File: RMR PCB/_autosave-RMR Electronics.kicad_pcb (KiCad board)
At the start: 2 copper layers, 19 parts, among them J4 RMotor, J8 RMotor Control

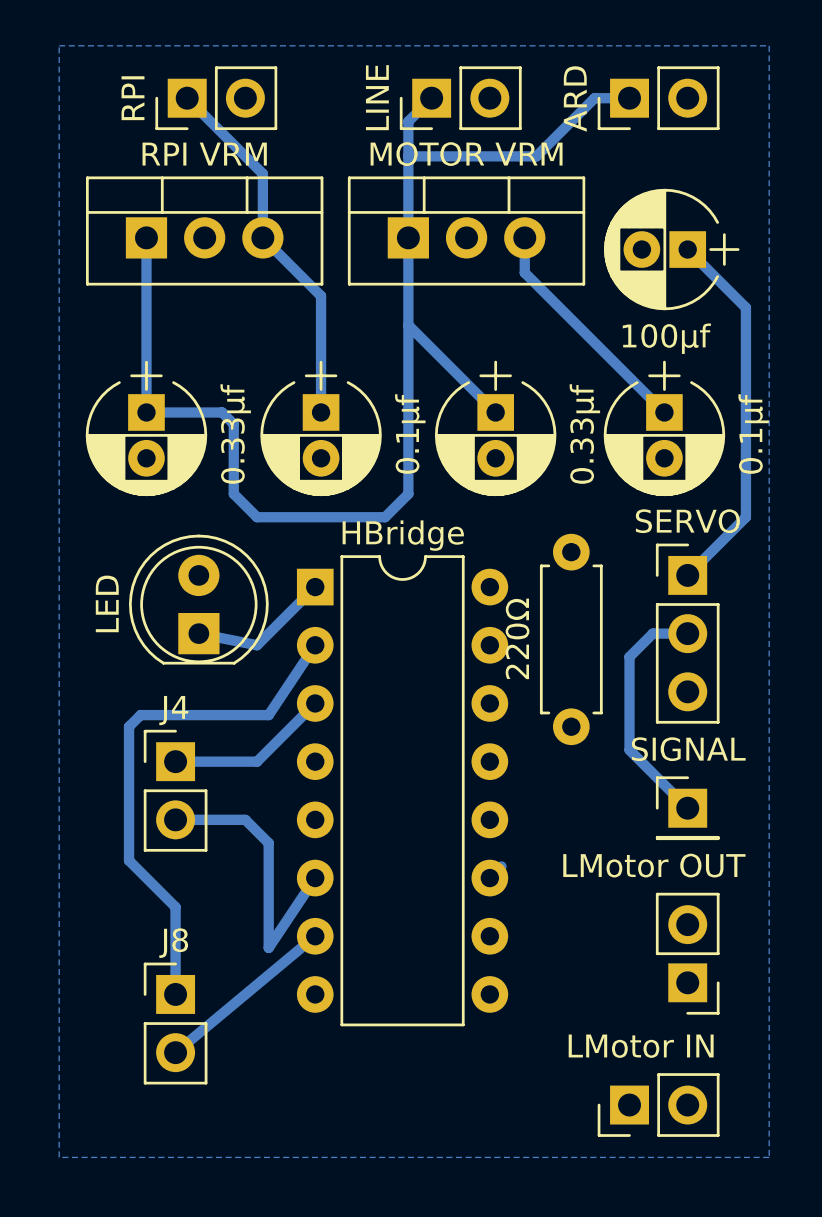
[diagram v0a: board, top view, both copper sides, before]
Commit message: reduced  PCB size drastically, outstanding GND copper pour issue
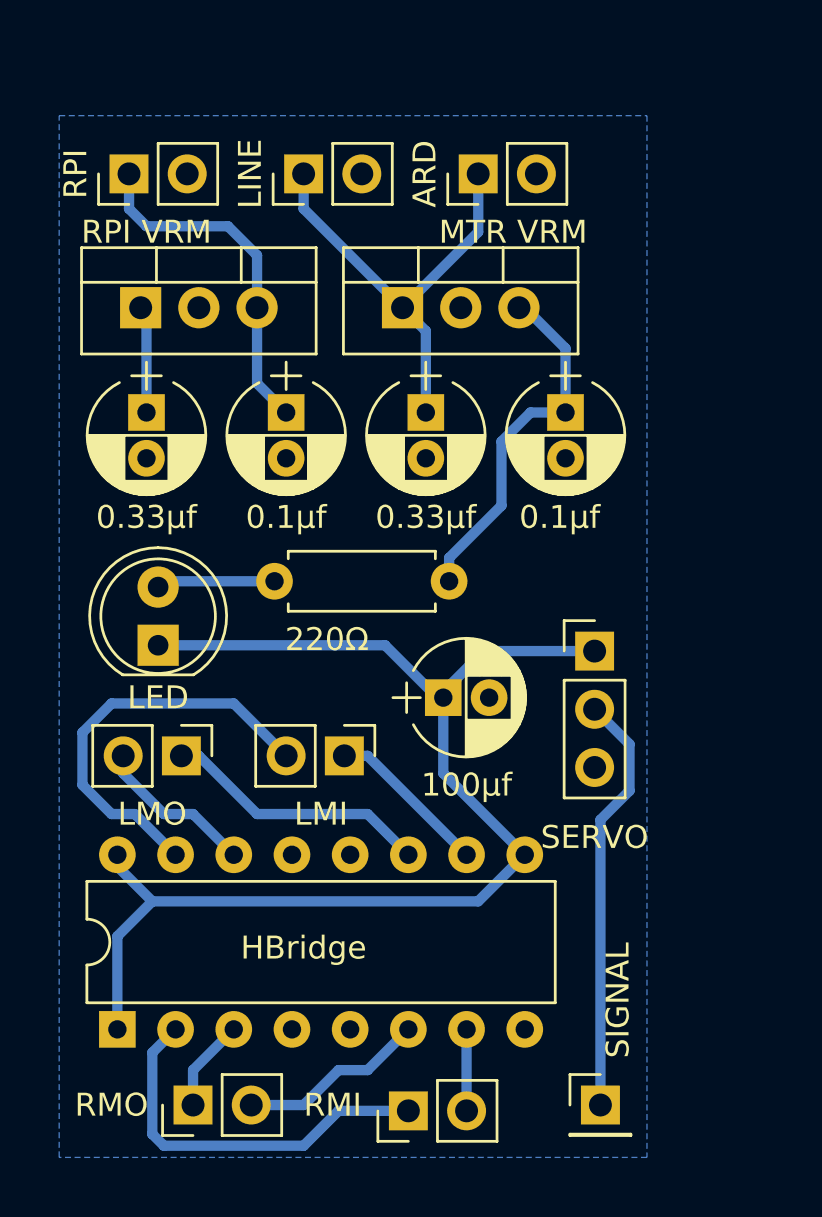
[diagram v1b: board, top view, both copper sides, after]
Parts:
- LMI: renamed from LMotor IN
- LMO: renamed from LMotor OUT
- MTR VRM: renamed from MOTOR VRM
- moved LMO 24.2 mm to (127.3, 109.0), turned to 270 degrees
- moved 100μf 22.3 mm to (138.7, 106.4), turned to 0 degrees
- moved HBridge 21.1 mm to (124.5, 120.9), turned to 90 degrees
- moved LMI 19.7 mm to (134.4, 109.0), turned to 270 degrees
- moved RMO 15.0 mm to (127.8, 124.2), turned to 90 degrees
- moved 220Ω 14.4 mm to (131.3, 101.3), turned to 0 degrees
- moved SIGNAL 13.5 mm to (145.5, 124.2)
- moved RMI 11.4 mm to (137.2, 124.5), turned to 90 degrees
- moved ARD 7.38 mm to (140.2, 83.6)
- moved LINE 6.49 mm to (132.6, 83.6)
- moved SERVO 5.24 mm to (145.3, 104.4)
- moved 0.1μf 4.32 mm to (144.0, 94.0)
- moved RPI 4.17 mm to (125.0, 83.6)
- moved RPI VRM 3.06 mm to (125.5, 89.4)
- moved MTR VRM 3.06 mm to (136.9, 89.4)
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- renumbered J8 to RMI, J4 to RMO
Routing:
- net Net-(C5-Pad1): track 22.5 -> 55.6 mm
- net Net-(C1-Pad1): track 56.9 -> 24.5 mm
- net Net-(H1-Pad15): track 0.51 -> 18.0 mm
- net Net-(H1-Pad11): track 0.72 -> 11.7 mm
- net Net-(J3-Pad2): track 10.6 -> 19.4 mm
- net Net-(H1-Pad10): track 0.00 -> 7.12 mm
- net Net-(H1-Pad14): track 0.00 -> 7.06 mm
- net Net-(C4-Pad1): track 10.1 -> 15.9 mm
- net Net-(H1-Pad2): track 22.5 -> 17.0 mm
- net Net-(D1-Pad2): track 0.00 -> 5.19 mm
- net Net-(H1-Pad7): track 7.94 -> 3.56 mm
- net Net-(H1-Pad6): track 12.7 -> 8.48 mm
- net Net-(H1-Pad3): track 7.15 -> 4.04 mm
- net Net-(C2-Pad1): track 16.1 -> 15.3 mm

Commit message: figured out that I am dumb
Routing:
- net Net-(C1-Pad1): track 24.5 -> 42.6 mm
- net Net-(C5-Pad1): track 55.6 -> 67.0 mm
- net Net-(C2-Pad1): track 15.3 -> 14.1 mm
- net Net-(H1-Pad15): track 18.0 -> 18.9 mm
- net Net-(C4-Pad1): track 15.9 -> 15.1 mm
- net Net-(H1-Pad11): track 11.7 -> 12.5 mm
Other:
- board outline added: 26.7 x 46.5 mm
